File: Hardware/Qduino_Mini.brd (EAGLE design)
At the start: 38.1 x 25.4 mm, 45 parts, among them Q1 PFET, U1 ATMEGA32U41:1-LESS_PASTE, U2 MCP73831, U3 MAX17048, U4 TPS78233, U7 DNP, Y1 8MHZ

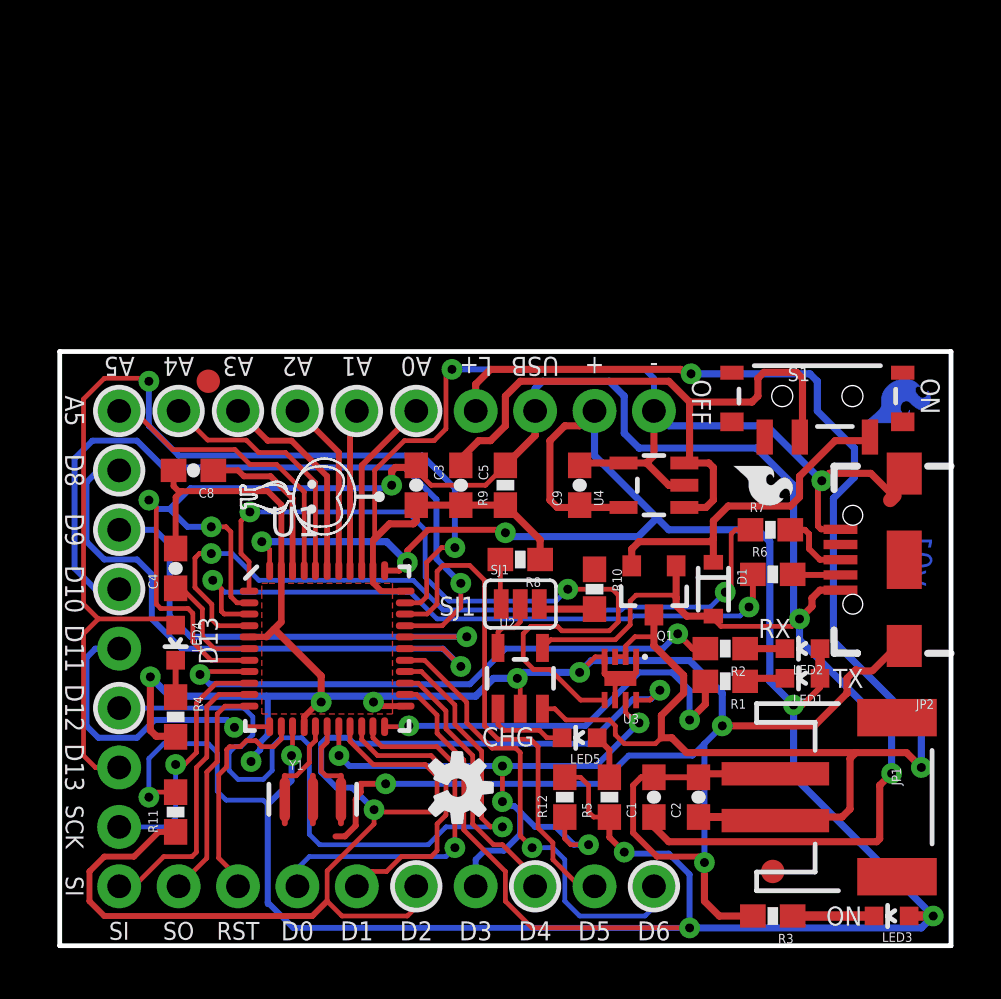
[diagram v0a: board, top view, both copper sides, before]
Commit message: Fixed library caused(?) inconsistencies
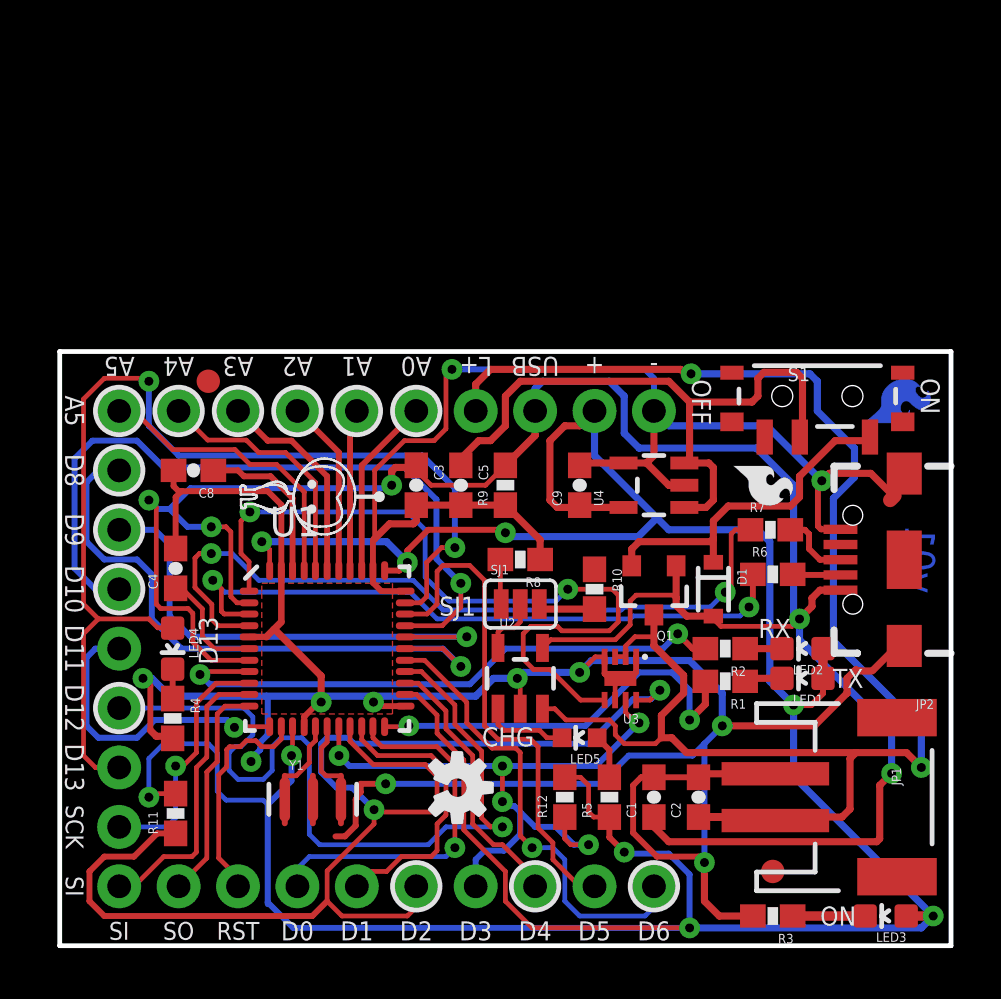
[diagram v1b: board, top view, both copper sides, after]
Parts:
- removed U$1: MIGHTYQ-S-SILK, Qtechknow:LOGO-SMALL-SILK
- removed U$5: MIGHTYQ-L-SILK, Qtechknow:LOGO-LARGE-SILK
- added U5: MIGHTYQ-L-SILK, SparkFun-Aesthetics:LOGO-LARGE-SILK
- added U6: MIGHTYQ-S-SILK, SparkFun-Aesthetics:LOGO-SMALL-SILK
- D1: value (none) -> BAS16JTR
- LED1, LED2, LED3, LED4: device SFE LED:LED-0603 -> SparkFun-LED:LED-0603
- S1: value (none) -> POWER
- U4: device Pinoccio:SOT23-5 -> SparkFun-PowerIC:SOT23-5
- U7: device Qduino_Mini:QDUINO_MINI_V14 -> SparkFun-Aesthetics:QDUINO_MINI_V15
- moved LED4 0.28 mm to (4.83, 12.7)
- moved LED3 0.25 mm to (35.3, 1.27)
- moved R4 0.14 mm to (4.83, 9.72)
- moved R11 0.06 mm to (4.95, 5.65)

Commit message: Added logos to sch, massaged silk & a trace
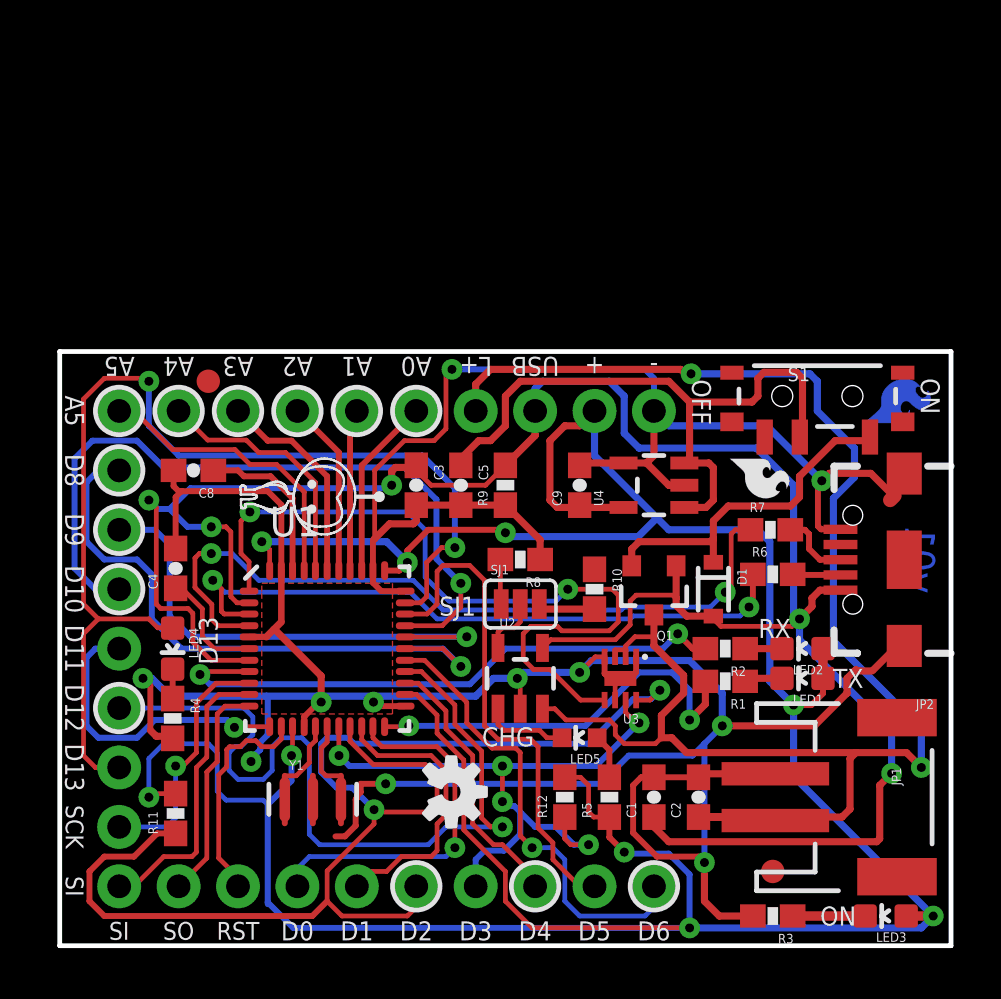
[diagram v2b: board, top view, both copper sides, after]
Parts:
- removed U$2: (no value), SparkFun-Aesthetics:SFE_LOGO_FLAME_.1
- removed U$3: (no value), SparkFun-Aesthetics:OSHW-LOGO-S
- added LOGO1: OSHW-LOGOS, SparkFun-Aesthetics:OSHW-LOGO-S
- added LOGO2: SFE_LOGO_FLAME.1_INCH, SparkFun-Aesthetics:SFE_LOGO_FLAME_.1
- U3: device Pinoccio:DFN-8 -> SparkFun-DigitalIC:DFN-8
- moved U5 2.77 mm to (18.8, 12.7)
- moved U3 1.51 mm to (24.0, 11.4)
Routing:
- net LIPO: track 73.9 -> 74.6 mm
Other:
- board text added: "Revised by: Brent Wilkins"
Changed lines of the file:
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@@
 <setting verticaltext="up"/>
 </settings>
-<grid distance="0.0025" unitdist="inch" unit="inch" style="lines" multiple="1" display="yes" altdistance="0.005" altunitdist="inch" altunit="inch"/>
+<grid distance="1" unitdist="mil" unit="mil" style="lines" multiple="1" display="yes" altdistance="0.25" altunitdist="mil" altunit="mil"/>
 <layers>
 <layer number="1" name="Top" color="4" fill="1" visible="yes" active="yes"/>
@@
 <wire x1="0" y1="0" x2="38.1" y2="0" width="0.2032" layer="20"/>
 <text x="15.1892" y="-9.3726" size="1.778" layer="51">&gt;DESIGNER</text>
-<dimension x1="0" y1="25.4" x2="38.1" y2="25.4" x3="19.05" y3="29.21" textsize="1.778" textratio="15" layer="51" unit="inch"/>
-<dimension x1="0" y1="25.4" x2="0" y2="0" x3="-3.81" y3="12.7" textsize="1.778" textratio="15" layer="51" unit="inch"/>
-<text x="5.08" y="33.02" size="1.778" layer="51" font="vector" ratio="15">All units in inches</text>
+<dimension x1="0" y1="25.4" x2="38.1" y2="25.4" x3="19.05" y3="29.21" textsize="1.778" textratio="15" layer="47" unit="inch"/>
+<dimension x1="0" y1="25.4" x2="0" y2="0" x3="-3.81" y3="12.7" textsize="1.778" textratio="15" layer="47" unit="inch"/>
+<text x="5.08" y="33.02" size="1.778" layer="47" font="vector" ratio="15">All units in inches</text>
 <text x="36.7792" y="16.51" size="1.27" layer="16" ratio="15" rot="MR270" align="center">&gt;VERSION</text>
 <text x="17.0053" y="14.5161" size="0.8128" layer="21" ratio="16" rot="SR0" align="center">SJ1</text>
+<text x="-4.1148" y="-11.8364" size="1.778" layer="51">Revised by: Brent Wilkins</text>
 </plain>
 <attributes>
@@
 <attribute name="PROD_ID" value="IC-10828" x="11.43" y="12.7" size="1.778" layer="27" display="off"/>
 </element>
-<element name="U$3" library="SparkFun-Aesthetics" package="OSHW-LOGO-S" value="" x="16.9926" y="6.7564" rot="R270"/>
 <element name="FRAME2" library="SparkFun-Aesthetics" package="CREATIVE_COMMONS" value="" x="-15.5702" y="-9.4234">
 <attribute name="VERSION" value="v01" x="-15.5702" y="-9.4234" size="1.778" layer="27" display="off"/>
@@
 <attribute name="PROD_ID" value="SWCH-10651" x="32.385" y="23.495" size="1.778" layer="27" display="off"/>
 </element>
-<element name="U3" library="Pinoccio" package="DFN-8" value="MAX17048" x="24.765" y="12.7" rot="R180">
-<attribute name="PROD_ID" value="IC-12551" x="24.765" y="12.7" size="1.778" layer="27" rot="R180" display="off"/>
+<element name="U3" library="SparkFun-DigitalIC" package="DFN-8" value="MAX17048" x="23.9522" y="11.43" rot="R180">
+<attribute name="PROD_ID" value="IC-12551" x="23.9522" y="11.43" size="1.778" layer="27" rot="R180" display="off"/>
 </element>
 <element name="U4" library="SparkFun-PowerIC" package="SOT23-5" value="TPS78233" x="25.4" y="19.685" rot="R90">
@@
 <attribute name="PROD_ID" value="DIO-09646" x="27.94" y="15.24" size="1.778" layer="27" rot="R270" display="off"/>
 </element>
-<element name="U5" library="SparkFun-Aesthetics" package="LOGO-LARGE-SILK" value="MIGHTYQ-L-SILK" x="21.59" y="12.7" rot="MR90"/>
+<element name="U5" library="SparkFun-Aesthetics" package="LOGO-LARGE-SILK" value="MIGHTYQ-L-SILK" x="18.8214" y="12.7" rot="MR90"/>
 <element name="U6" library="SparkFun-Aesthetics" package="LOGO-SMALL-SILK" value="MIGHTYQ-S-SILK" x="10.033" y="19.177" rot="R270"/>
 <element name="SJ1" library="SparkFun-Passives" package="PAD-JUMPER-3-2OF3_NC_BY_PASTE_YES_SILK_FULL_BOX" value="" x="19.685" y="14.605" rot="SR0"/>
@@
 <attribute name="VALUE" value="10K" x="22.86" y="15.24" size="1.778" layer="27" rot="R270" display="off"/>
 </element>
-<element name="U$2" library="SparkFun-Aesthetics" package="SFE_LOGO_FLAME_.1" value="" x="28.448" y="20.828" rot="R270"/>
 <element name="U$6" library="SparkFun-Aesthetics" package="SFE-LOGO-FLAME-COPPER" value="" x="34.417" y="22.352" rot="MR90"/>
 <element name="R11" library="SparkFun-Passives" package="0603-RES" value="4.7K" x="4.953" y="5.6515" rot="R90">
@@
 <attribute name="PROD_ID" value="XTAL-08895" x="10.8204" y="6.2484" size="1.778" layer="27" display="off"/>
 </element>
+<element name="LOGO1" library="SparkFun-Aesthetics" package="OSHW-LOGO-S" value="OSHW-LOGOS" x="16.7386" y="6.5786" rot="R270"/>
+<element name="LOGO2" library="SparkFun-Aesthetics" package="SFE_LOGO_FLAME_.1" value="SFE_LOGO_FLAME.1_INCH" x="28.2956" y="21.1328" rot="R270"/>
 </elements>
 <signals>
@@
 <wire x1="33.0708" y1="13.0302" x2="33.0708" y2="19.1262" width="0.3048" layer="16"/>
 <wire x1="33.0708" y1="19.1262" x2="33.9725" y2="20.0279" width="0.3048" layer="16"/>
-<wire x1="23.749" y1="12.359" x2="24.181" y2="12.359" width="0.2032" layer="1"/>
 <wire x1="25.7175" y1="8.89" x2="25.7175" y2="9.8425" width="0.3048" layer="1"/>
 <wire x1="25.7175" y1="9.8425" x2="26.67" y2="10.795" width="0.3048" layer="1"/>
@@
 <wire x1="24.19" y1="12.8108" x2="24.19" y2="12.35" width="0.2032" layer="1"/>
 <wire x1="24.181" y1="12.359" x2="24.19" y2="12.35" width="0.2032" layer="1"/>
+<wire x1="24.181" y1="12.359" x2="24.181" y2="12.35" width="0.2032" layer="1"/>
+<wire x1="24.19" y1="12.6492" x2="23.74" y2="12.6492" width="0.2032" layer="1"/>
+<wire x1="23.74" y1="12.6492" x2="23.74" y2="12.35" width="0.2032" layer="1"/>
+<wire x1="24.2062" y1="12.6492" x2="24.19" y2="12.6492" width="0.2032" layer="1"/>
+<wire x1="24.19" y1="12.6492" x2="24.19" y2="12.35" width="0.2032" layer="1"/>
 </signal>
 <signal name="VCC">

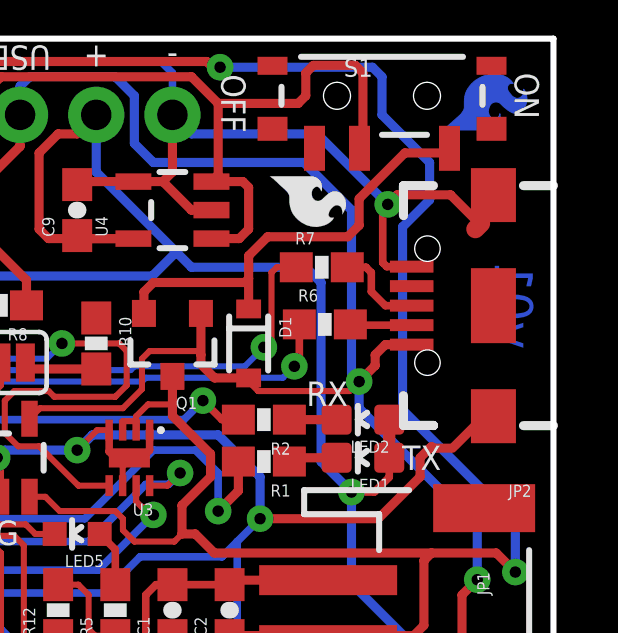
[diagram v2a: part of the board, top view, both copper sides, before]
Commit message: Added vias to USB connector pads to improve mechanical strength (from what I hear)
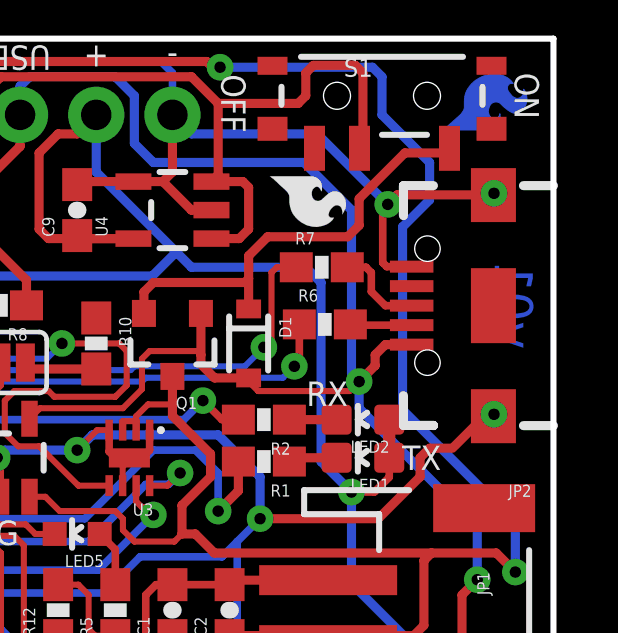
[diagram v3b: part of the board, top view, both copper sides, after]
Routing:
- net GND: track 168.7 -> 168.4 mm, vias 11 -> 13
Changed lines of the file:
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@@
 <setting verticaltext="up"/>
 </settings>
-<grid distance="1" unitdist="mil" unit="mil" style="lines" multiple="1" display="yes" altdistance="0.25" altunitdist="mil" altunit="mil"/>
+<grid distance="0.05" unitdist="inch" unit="inch" style="lines" multiple="1" display="yes" altdistance="0.25" altunitdist="mil" altunit="mil"/>
 <layers>
 <layer number="1" name="Top" color="4" fill="1" visible="yes" active="yes"/>
@@
 <contactref element="U3" pad="P$4"/>
 <contactref element="R9" pad="1"/>
-<wire x1="35.497" y1="19.05" x2="35.68725" y2="19.24025" width="0.6096" layer="1"/>
 <wire x1="23.965" y1="11.425" x2="23.965" y2="11.392" width="0.254" layer="1"/>
 <wire x1="23.965" y1="11.392" x2="23.749" y2="11.176" width="0.254" layer="1"/>
@@
 <wire x1="33.655" y1="10.795" x2="33.655" y2="11.43" width="0.3048" layer="1"/>
 <wire x1="33.655" y1="11.43" x2="33.9725" y2="11.7475" width="0.3048" layer="1"/>
-<wire x1="33.9725" y1="11.7475" x2="34.0995" y2="11.7475" width="0.3048" layer="1"/>
-<wire x1="34.0995" y1="11.7475" x2="34.7345" y2="11.7475" width="0.3048" layer="1"/>
-<wire x1="34.036" y1="11.811" x2="34.0995" y2="11.7475" width="0.3048" layer="1"/>
+<wire x1="33.9725" y1="11.7475" x2="34.7345" y2="11.7475" width="0.3048" layer="1"/>
 <wire x1="35.624" y1="12.637" x2="34.798" y2="11.811" width="0.3048" layer="1"/>
 <wire x1="13.43" y1="17.367" x2="13.462" y2="17.399" width="0.3048" layer="1"/>
@@
 <wire x1="20.535" y1="17.35" x2="19.05" y2="18.835" width="0.3048" layer="1"/>
 <via x="32.5755" y="19.8755" extent="1-16" drill="0.381"/>
-<wire x1="35.68725" y1="19.24025" x2="35.62375" y2="19.24025" width="0.3048" layer="1"/>
-<wire x1="35.62375" y1="19.24025" x2="34.671" y2="20.193" width="0.3048" layer="1"/>
-<wire x1="34.671" y1="20.193" x2="32.893" y2="20.193" width="0.3048" layer="1"/>
+<wire x1="36.1188" y1="20.193" x2="32.893" y2="20.193" width="0.3048" layer="1"/>
 <wire x1="32.893" y1="20.193" x2="32.5755" y2="19.8755" width="0.3048" layer="1"/>
 <wire x1="34.798" y1="11.811" x2="34.7345" y2="11.7475" width="0.2032" layer="1"/>
@@
 <wire x1="3.556" y1="11.43" x2="3.937" y2="11.43" width="0.3048" layer="16"/>
 <wire x1="3.937" y1="11.43" x2="4.699" y2="10.668" width="0.3048" layer="16"/>
+<via x="36.1188" y="20.2438" extent="1-16" drill="0.381"/>
+<via x="36.1188" y="12.8778" extent="1-16" drill="0.381"/>
+<wire x1="36.1188" y1="20.193" x2="36.1188" y2="20.2438" width="0.3048" layer="1"/>
 </signal>
 <signal name="RST">

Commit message: Complete rework
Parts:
- removed FID5, FID6: FIDUCIAL1X2, SparkFun-Aesthetics:FIDUCIAL-1X2
- removed LED5: CRG / RED, SparkFun:LED-0603
- removed R1, R3, R4: 330, SparkFun-Resistors:0603-RES
- removed U$6: (no value), SparkFun-Aesthetics:SFE-LOGO-FLAME-COPPER
- removed U6: MIGHTYQ-S-SILK, SparkFun-Aesthetics:LOGO-SMALL-SILK
- removed U7: DNP, SparkFun-Aesthetics:QDUINO_MINI_V15
- added FID1, FID2: FIDUCIALUFIDUCIAL, SparkFun-Aesthetics:MICRO-FIDUCIAL
- added JP3, JP4: (no value), SparkFun-Connectors:1X12
- added LOGO3: SFE_LOGO_FLAME.1_INCH, SparkFun-Aesthetics:SFE_LOGO_FLAME_.1@1
- D1: value BAS16JTR -> 250mA/100V
- JP2: value USB_MICROB_PLUGCONN-11752 -> (none)
- LED1: value TX / YLW -> (none); device SparkFun-LED:LED-0603 -> Spark:PLCC4-2MM-RGB
- LED2: value RX / GRN -> (none); device SparkFun-LED:LED-0603 -> Spark:PLCC4-2MM-RGB
- R2, R5: device SparkFun-Resistors:0603-RES -> SparkFun-Passives:0603-ARV
- U4: value TPS78233 -> AP2112K-3.3TRG-1
- moved LED3 33.9 mm to (15.2, 28.6), turned to 180 degrees
- moved C2 32.3 mm to (8.26, 32.4), turned to 270 degrees
- moved C1 30.5 mm to (9.53, 32.4)
- moved S1 30.4 mm to (5.08, 36.8)
- moved JP2 29.1 mm to (14.6, 36.1), turned to 270 degrees
- moved LED2 28.7 mm to (8.26, 29.2)
- moved LOGO2 28.4 mm to (3.17, 34.3), flipped to the bottom, turned to 0 degrees
- moved D1 27.6 mm to (6.35, 32.4)
- moved Q1 27.6 mm to (3.81, 32.4), turned to 90 degrees
- moved LED1 26.5 mm to (12.1, 29.2)
- moved R5 25.4 mm to (8.26, 26.7), turned to 0 degrees
- moved JP1 24.3 mm to (10.2, 3.81), turned to 180 degrees
- moved U2 22.5 mm to (5.08, 28.6), turned to 180 degrees
- moved R7 21.6 mm to (13.3, 31.1)
- moved R2 21.5 mm to (12.1, 26.7), turned to 0 degrees
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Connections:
- removed net N$12: LED3.C, R3.1
- new net N$32: LED2.BLUE, R5.6
- new net N$34: LED1.GREEN, R2.7
- new net N$35: LED2.RED, R5.8
- new net N$37: LED2.GREEN, R5.7
- net A0: now also JP3.7; no longer U7.A0
- net A1: now also JP3.8; no longer U7.A1
- net A2: now also JP3.9; no longer U7.A2
- net A3: now also JP3.10; no longer U7.A3
- net A4: now also JP3.11; no longer U7.A4
- net A5: now also JP3.12; no longer U7.A5
- net D10: now also R5.2; no longer U7.D10
- net D11: now also R5.3; no longer U7.D11
- net D12: now also JP3.6; no longer U7.D12
- net D13: now also R5.1; no longer LED4.A, U7.D31
- net D4: now also JP4.5; no longer U7.D4
- net D5: now also JP4.6; no longer U7.D5
- net D6: now also JP3.3; no longer U7.D6
- net D8: now also JP3.4; no longer U7.D8
- net D9: now also JP3.5; no longer U7.D9
- net GND: now also JP3.2, R2.4, R5.5; no longer R3.2, R4.2, U7.GND
- net LIPO: now also JP4.7; no longer U7.LIPO
- net MISO: now also JP4.10; no longer U7.MISO
- net MOSI: now also JP4.11; no longer U7.MOSI
- net N$1: now also LED1.RED, R2.8; no longer LED1.C, R1.1
- net N$2: now also LED1.BLUE, R2.6; no longer LED2.C, R2.1
- net N$4: now also LED3.C, R5.4; no longer LED5.A, R5.2
- net N$5: now also R2.5; no longer R4.1
- net RST: now also JP4.9; no longer U7.RST
- net RX: now also JP4.1; no longer U7.TX
- net RXLED: now also R2.3, U1.22; no longer R2.2, U1.8
- net SCK: now also JP4.12, LED4.A; no longer U7.SCK
- net SCL: now also JP4.4; no longer U7.D3
- net SDA: now also JP4.3; no longer U7.D2
- net STAT: now also R2.1; no longer LED5.C
- net TX: now also JP4.2; no longer U7.RX
- net TXLED: now also R2.2, U1.8; no longer R1.2, U1.22
- net VBUS: now also JP4.8; no longer U7.VUSB
- net VCC: now also JP3.1, LED1.CA, LED2.CA; no longer LED1.A, LED2.A, R5.1, U7.VCC
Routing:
- net SDA: track 56.3 -> 23.4 mm, vias 2 -> 1
- net N$5: track 1.26 -> 31.5 mm, vias 0 -> 2
- net D12: track 35.4 -> 11.7 mm, vias 1 -> 2
- net LIPO: track 74.6 -> 52.1 mm, vias 2 -> 6
- net VINPUT: track 27.8 -> 49.6 mm, vias 0 -> 2
- net D13: track 46.6 -> 26.1 mm
- net VCC: track 142.9 -> 122.8 mm, vias 9 -> 11
- net VBUS: track 98.6 -> 80.2 mm, vias 5 -> 9
- net GND: track 168.4 -> 151.1 mm, vias 13 -> 8
- net UCAP: track 4.91 -> 21.7 mm, vias 0 -> 4
- net D8: track 26.2 -> 12.0 mm
- net D10: track 31.5 -> 18.7 mm, vias 1 -> 2
- net D+: track 32.2 -> 20.6 mm
- net D9: track 21.2 -> 9.62 mm
- net SCL: track 28.8 -> 17.2 mm, vias 5 -> 1
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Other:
- board size 38.1 x 25.4 mm -> 20.3 x 38.1 mm
- board text added: "A0"
- board text added: "A1"
- board text added: "A2"
- board text added: "A3"
- board text added: "A4"
- board text added: "A5"
- board text added: "D0"
- board text added: "D1"
- board text added: "D12"
- board text added: "D15"
- board text added: "D16"
- board text added: "D17"
- board text added: "D2"
- board text added: "D3"
- board text added: "D4"
- board text added: "D5"
- board text added: "D6"
- board text added: "D8"
- board text added: "D9"
- board text added: "GND"
- board text added: "L+"
- board text added: "LIPO"
- board text added: "MISO"
- board text added: "MOSI"
- board text added: "RST"
- board text added: "SCK"
- board text added: "SCL"
- board text added: "SDA"
- board text added: "USB"
- board text added: "VCC"
- board text removed: "All units in inches"
- board text removed: "CHG"
- board text removed: "D13"
- board text removed: "OFF"
- board text removed: "ON"
- board text removed: "SJ1"
